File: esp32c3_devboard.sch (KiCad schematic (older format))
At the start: 0 parts

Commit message: Update schematic with ESP32 module, power supply and USB to serial
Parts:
- added C? (x5): 0.1uF, symbol Device:C_Small
- added C? (x2): 1uF, symbol Device:C_Small
- added C? (x3): 10uF, symbol Device:C_Small
- added D? (x2): D_Schottky, symbol Device:D_Schottky_Small
- added D?: YELLOW_LED, symbol Device:LED_Small
- added D?: RED_LED, symbol Device:LED_Small
- added J?: UART USB, symbol Connector:USB_B_Micro
- added J?: JTAG USB, symbol Connector:USB_B_Micro
- added J? (x2): Conn_01x15_Male, symbol Connector_Generic:Conn_01x15
- added R?: 10K, symbol Device:R_Small
- added R?: 800R, symbol Device:R_Small
- added R?: 1.7K, symbol Device:R_Small
- added SW? (x2): RSTn, symbol Switch:SW_Push
- added TP? (x12): TestPoint, symbol Connector:TestPoint
- added U?: ESP32-C3-MINI-1, Espressif:ESP32-C3-MINI-1, symbol Espressif:ESP32-C3-MINI-1
- added U?: AMS1117, Package_TO_SOT_SMD:SOT-223-3_TabPin2, symbol Regulator_Linear:AMS1117-3.3
- added U?: CH340E, Package_SO:MSOP-10_3x3mm_P0.5mm, symbol Interface_USB:CH340E
- added U?: SRV05-4, Package_TO_SOT_SMD:SOT-23-6, symbol Power_Protection:SRV05-4
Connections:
- new net: C?.1, U?.10 (V3)
- new net: D?.2 (A), R?.2 (x2)
- new net +3V3: C?.1, C?.1, C?.1, C?.1, J?.2 (Pin_2), J?.3 (Pin_3), R?.1, R?.1, TP?.1, U?.2 (VO), U?.3 (3V3)
- new net +5VL: D?.2 (A), J?.1 (VBUS), TP?.1
- new net +5VP: D?.2 (A), J?.1 (VBUS), TP?.1
- new net CHIP_PU: C?.1, J?.7 (Pin_7), R?.2, SW?.2, TP?.1, U?.8 (EN/CHIP_PU)
- new net GND: C?.2, C?.2, C?.2, C?.2, C?.2, C?.2, C?.2, C?.2, C?.2, C?.2, D?.1 (K), D?.1 (K), J?.1 (Pin_1), J?.1 (Pin_1), J?.12 (Pin_12), J?.12 (Pin_12), J?.15 (Pin_15), J?.15 (Pin_15), J?.4 (Pin_4), J?.5 (GND), J?.5 (GND), J?.6 (Pin_6), J?.7 (Pin_7), J?.8 (Pin_8), SW?.1, SW?.1, U?.1 (GND), U?.1 (GND), U?.11 (GND), U?.14 (GND), U?.2 (GND), U?.2 (VN), U?.3 (GND), U?.36 (GND)
- new net GPIO0: J?.9 (Pin_9), U?.12 (GPIO0/ADC1_CH0/XTAL_32K_P)
- new net GPIO1: J?.10 (Pin_10), U?.13 (GPIO1/ADC1_CH1/XTAL_32K_N)
- new net GPIO10: J?.11 (Pin_11), U?.16 (GPIO10)
- new net GPIO18: J?.13 (Pin_13), J?.2 (D-), U?.26 (GPIO18/USB_D-), U?.6 (IO4)
- new net GPIO19: J?.14 (Pin_14), J?.3 (D+), U?.27 (GPIO19/USB_D+), U?.4 (IO3)
- new net GPIO2: J?.4 (Pin_4), TP?.1, U?.5 (GPIO2/ADC1_CH2)
- new net GPIO3: J?.5 (Pin_5), U?.6 (GPIO3/ADC1_CH3)
- new net GPIO4: J?.11 (Pin_11), U?.18 (GPIO4/ADC1_CH4)
- new net GPIO5: J?.10 (Pin_10), U?.19 (GPIO5/ADC2_CH0)
- new net GPIO6: J?.9 (Pin_9), U?.20 (GPIO6)
- new net GPIO7: J?.8 (Pin_8), U?.21 (GPIO7)
- new net GPIO8: J?.6 (Pin_6), R?.1, TP?.1, U?.22 (GPIO8)
- new net GPIO9: J?.5 (Pin_5), SW?.2, TP?.1, U?.23 (GPIO9)
- new net RXD_3V3: J?.3 (Pin_3), TP?.1, U?.30 (GPIO20/U0RXD)
- new net RXD_5V: TP?.1, U?.9 (RXD)
- new net TXD_3V3: J?.2 (Pin_2), TP?.1, U?.31 (GPIO21/U0TXD)
- new net TXD_5V: TP?.1, U?.8 (TXD)
- new net UART_USB_D+: J?.3 (D+), U?.1 (IO1), U?.1 (UD+)
- new net UART_USB_D-: J?.2 (D-), U?.2 (UD-), U?.3 (IO2)
- new net VCC: C?.1, C?.1, C?.1, C?.1, D?.1 (K), D?.1 (K), J?.13 (Pin_13), J?.14 (Pin_14), TP?.1, U?.3 (VI), U?.5 (VP), U?.7 (VCC)
- no-connect marks 0 -> 21
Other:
- note added: "2 mA LED current"
- note added: "5V to 3.3V LDO"
- note added: "ESP32-C3-MINI-1 module"
- note added: "Input power supply selection"
- note added: "JTAG USB connector"
- note added: "Pin headers"
- note added: "Power indicator LED"
- note added: "Power supply test points:"
- note added: "Reset button"
- note added: "Strapping pins"
- note added: "Strapping pins test points:"
- note added: "Test points"
- note added: "UART 5V to 3.3V level shifter"
- note added: "UART USB connector"
- note added: "UART test points:"
- note added: "USB ESD protection"
- note added: "USB to UART"
- note added: "User LED and button"

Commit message: Place components on PCB
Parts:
- removed C? (x2): 0.1uF, symbol Device:C_Small
- removed C?: 1uF, symbol Device:C_Small
- removed TP? (x2): TestPoint, symbol Connector:TestPoint
- removed U?: CH340E, Package_SO:MSOP-10_3x3mm_P0.5mm, symbol Interface_USB:CH340E
- added C10: 10uF, Capacitor_SMD:C_0805_2012Metric, symbol Device:C_Small
- added C8: 1uF, Capacitor_SMD:C_0402_1005Metric, symbol Device:C_Small
- added C9: 0.1uF, Capacitor_SMD:C_0402_1005Metric, symbol Device:C_Small
- added NT1: Net-Tie_3, NetTie:NetTie-3_SMD_Pad2.0mm, symbol Device:Net-Tie_3
- added R3: 10K, Resistor_SMD:R_0603_1608Metric, symbol Device:R_Small
- added R5: 24K, Resistor_SMD:R_0603_1608Metric, symbol Device:R_Small
- added R6: 47K, Resistor_SMD:R_0603_1608Metric, symbol Device:R_Small
- added R7: 4K7, Resistor_SMD:R_0603_1608Metric, symbol Device:R_Small
- added U4: CP2102N-A01-GQFN28, Package_DFN_QFN:QFN-28-1EP_5x5mm_P0.5mm_EP3.35x3.35mm, symbol Interface_USB:CP2102N-A01-GQFN28
- C1, C4, C7: renamed from C?; footprint (none) -> Capacitor_SMD:C_0805_2012Metric
- C2, C3: renamed from C?; footprint (none) -> Capacitor_SMD:C_0402_1005Metric
- C5, C6: renamed from C?; footprint (none) -> Capacitor_SMD:C_0603_1608Metric
- D1, D2: renamed from D?; footprint (none) -> Diode_SMD:D_SOD-323
- D3, D4: renamed from D?; footprint (none) -> LED_SMD:LED_0805_2012Metric
- J1, J2: renamed from J?; footprint (none) -> Connector_USB:USB_Micro-B_Molex-105017-0001
- J3, J4: renamed from J?; footprint (none) -> Connector_PinHeader_2.54mm:PinHeader_1x15_P2.54mm_Vertical
- R1: renamed from R?; footprint (none) -> Resistor_SMD:R_0603_1608Metric
- R2: renamed from R?; value 800R -> 1K; footprint (none) -> Resistor_SMD:R_0603_1608Metric
- R4: renamed from R?; value 1.7K -> 1.1K; footprint (none) -> Resistor_SMD:R_0603_1608Metric
- SW1: renamed from SW?; value RSTn -> SW_RSTN; footprint (none) -> Button_Switch_SMD:SW_Push_1P1T_NO_6x6mm_H9.5mm
- SW2: renamed from SW?; value RSTn -> SW_USR; footprint (none) -> Button_Switch_SMD:SW_Push_1P1T_NO_6x6mm_H9.5mm
- TP1: renamed from TP?; value TestPoint -> TP_5V_UART_USB; footprint (none) -> TestPoint:TestPoint_Pad_D1.0mm
- TP10: renamed from TP?; value TestPoint -> TP_BOOT_GPIO9; footprint (none) -> TestPoint:TestPoint_Pad_D1.0mm
- TP2: renamed from TP?; value TestPoint -> TP_5V_JTAG_USB; footprint (none) -> TestPoint:TestPoint_Pad_D1.0mm
- TP3: renamed from TP?; value TestPoint -> TP_5V; footprint (none) -> TestPoint:TestPoint_Pad_D1.0mm
- TP4: renamed from TP?; value TestPoint -> TP_3V3; footprint (none) -> TestPoint:TestPoint_Pad_D1.0mm
- TP5: renamed from TP?; value TestPoint -> TP_UART_TXD; footprint (none) -> TestPoint:TestPoint_Pad_D1.0mm
- TP6: renamed from TP?; value TestPoint -> TP_UART_RXD; footprint (none) -> TestPoint:TestPoint_Pad_D1.0mm
- TP7: renamed from TP?; value TestPoint -> TP_CHIP_PU; footprint (none) -> TestPoint:TestPoint_Pad_D1.0mm
- TP8: renamed from TP?; value TestPoint -> TP_BOOT_GPIO2; footprint (none) -> TestPoint:TestPoint_Pad_D1.0mm
- TP9: renamed from TP?; value TestPoint -> TP_BOOT_GPIO8; footprint (none) -> TestPoint:TestPoint_Pad_D1.0mm
- gave numbers to parts that had none: 3
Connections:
- net RXD_5V is gone; now on net RXD: TP6.1
- net TXD_5V is gone; now on net TXD: TP5.1
- net +3V3: now also C10.1, C9.1, R3.1, R7.1, U4.6 (VDD), U4.7 (REGIN)
- net +5VP: now also R5.1
- net CHIP_PU: now also U4.24 (~RTS)
- net GND: now also C10.2, C8.2, C9.2, NT1.2, R6.2, U4.29 (GND), U4.3 (GND); no longer J1.5 (GND), J2.5 (GND)
- net GPIO8: now also R3.2
- net UART_USB_D+: now also U2.6 (IO4), U4.4 (D+); no longer U2.1 (IO1)
- net UART_USB_D-: now also U2.4 (IO3), U4.5 (D-); no longer U2.3 (IO2)
- net YELLOW_LED_PU: now reaches D4.2 (A), R4.2
- net RED_LED_PU: now reaches D3.2 (A), R2.2
- net GPIO18 renamed JTAG_USB_D-
- net JTAG_USB_D-: now also U2.1 (IO1); no longer U2.6 (IO4)
- net GPIO19 renamed JTAG_USB_D+
- net JTAG_USB_D+: now also U2.3 (IO2); no longer U2.4 (IO3)
- net GPIO9 renamed DTR
- net DTR: now also U4.28 (~DTR)
- net RXD_3V3 renamed RXD
- net RXD: now also U4.26 (TXD)
- net TXD_3V3 renamed TXD
- net TXD: now also U4.25 (RXD)
- net VCC renamed +5V
- new net GND1: J1.5 (GND), NT1.3
- new net GND2: J2.5 (GND), NT1.1
- new net RSTb: R7.2, U4.9 (~RSTb)
- new net VBUS: C8.1, R5.2, R6.1, U4.8 (VBUS)
- no-connect marks 21 -> 34
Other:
- note added: "GPIO8 needs to be pulled up\nin order to enter bootloader"
- note added: "Power indication LED"
- note added: "RTS should be connected to CHIP_PU\n\nDTR should be connected to GPIO9"
- note added: "TXD and RXD crossover intentional"
- note added: "UART_USB and JTAG_USB grounds are tied"
- note added: "Voltage divider needed for limiting VBUS\nvoltage when 3V3 is not connected\n\nCapacitor is here to delay rising of VBUS\nvoltage until LDO enables the 3V3 output"
- note removed: "Power indicator LED"
- note removed: "UART 5V to 3.3V level shifter"
- moved on the sheet: C3, C4, C5, C6, C7, D1, D2, D3, D4, J1, J3, J4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

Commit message: Add pullup on GPIO2 strapping pin
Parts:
- added R8: 10K, Resistor_SMD:R_0603_1608Metric, symbol Device:R_Small
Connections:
- net +3V3: now also R8.1
- net GPIO2: now also R8.2
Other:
- note added: "GPIO2 should be pulled up\n\nRTS should be connected to CHIP_PU\n\nDTR should be connected to GPIO9"
- note removed: "RTS should be connected to CHIP_PU\n\nDTR should be connected to GPIO9"
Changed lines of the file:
@@
 Text GLabel 2550 7050 0    35   Input ~ 0
 DTR
-Text Notes 2250 6450 0    31   ~ 0
-RTS should be connected to CHIP_PU\n\nDTR should be connected to GPIO9
 Text Notes 9950 4100 0    31   ~ 0
 TXD and RXD crossover intentional
@@
 Text Label 5900 7050 0    35   ~ 0
 YELLOW_LED_PU
+$Comp
+L Device:R_Small R8
+U 1 1 6332661E
+P 3200 6550
+F 0 "R8" H 3250 6650 35  0000 L CNN
+F 1 "10K" H 3250 6500 35  0000 L CNN
+F 2 "Resistor_SMD:R_0603_1608Metric" H 3200 6550 50  0001 C CNN
+F 3 "~" H 3200 6550 50  0001 C CNN
+	1    3200 6550
+	1    0    0    -1
+$EndComp
+$Comp
+L power:+3.3V #PWR06
+U 1 1 63326CD9
+P 3200 6400
+F 0 "#PWR06" H 3200 6250 50  0001 C CNN
+F 1 "+3.3V" H 3200 6550 35  0000 C CNN
+F 2 "" H 3200 6400 50  0001 C CNN
+F 3 "" H 3200 6400 50  0001 C CNN
+	1    3200 6400
+	1    0    0    -1
+$EndComp
+Text Notes 2100 6550 0    31   ~ 0
+GPIO2 should be pulled up\n\nRTS should be connected to CHIP_PU\n\nDTR should be connected to GPIO9
+Wire Wire Line
+	3200 6650 3400 6650
+Wire Wire Line
+	3200 6400 3200 6450
 $EndSCHEMATC

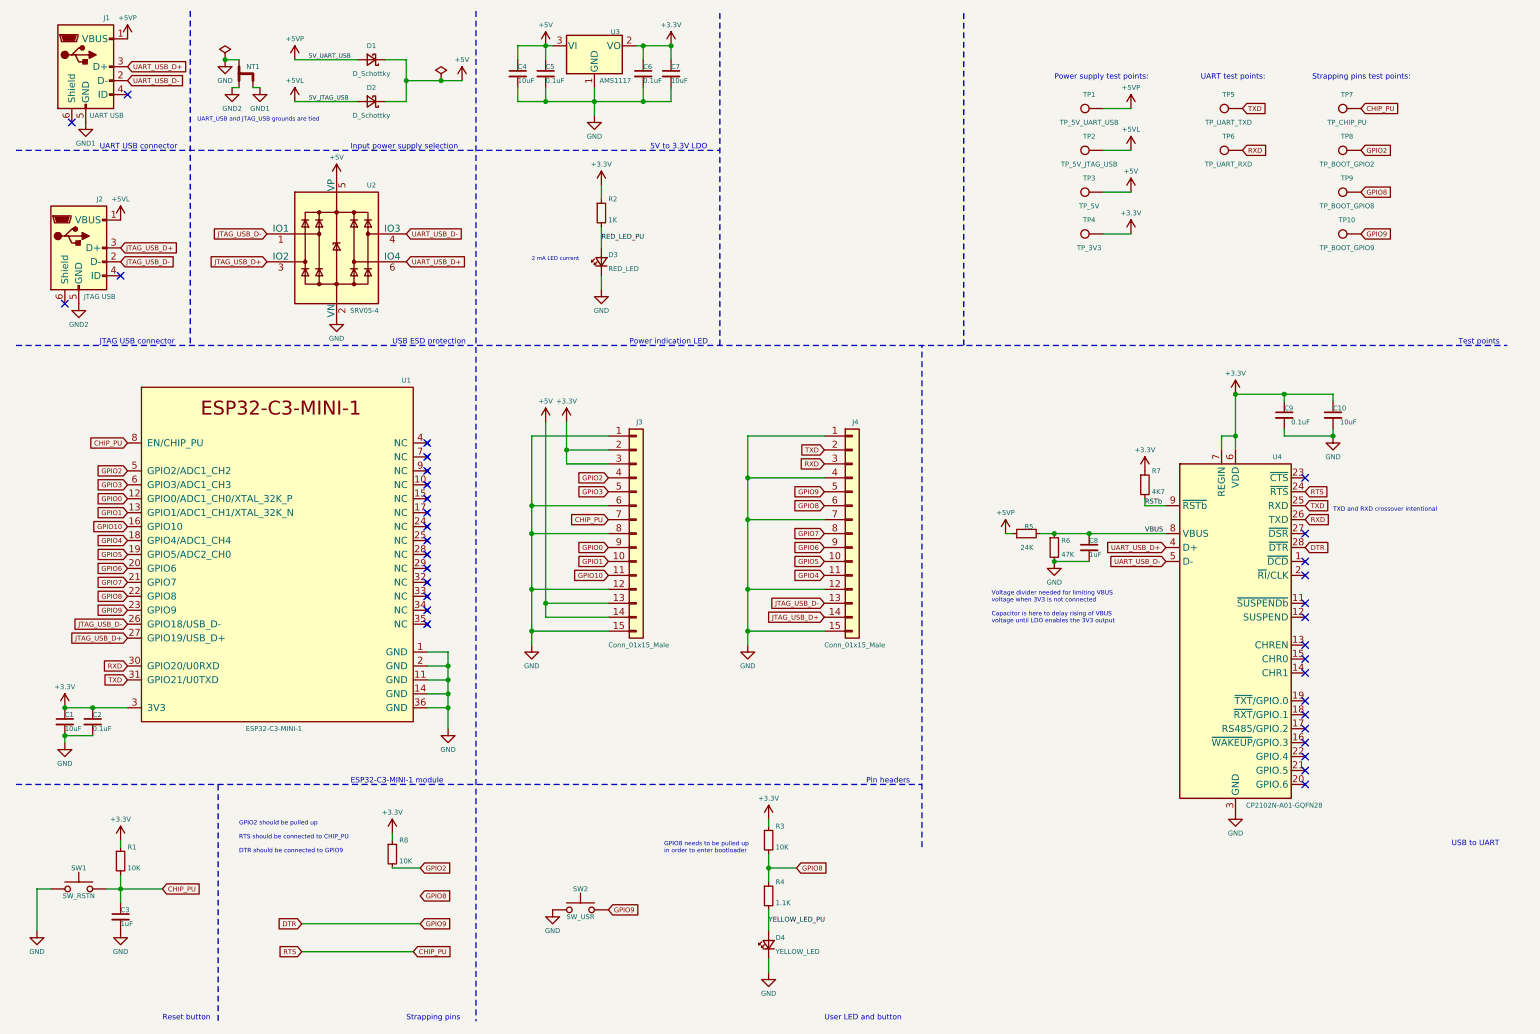
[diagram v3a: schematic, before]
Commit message: Add micro USB step files
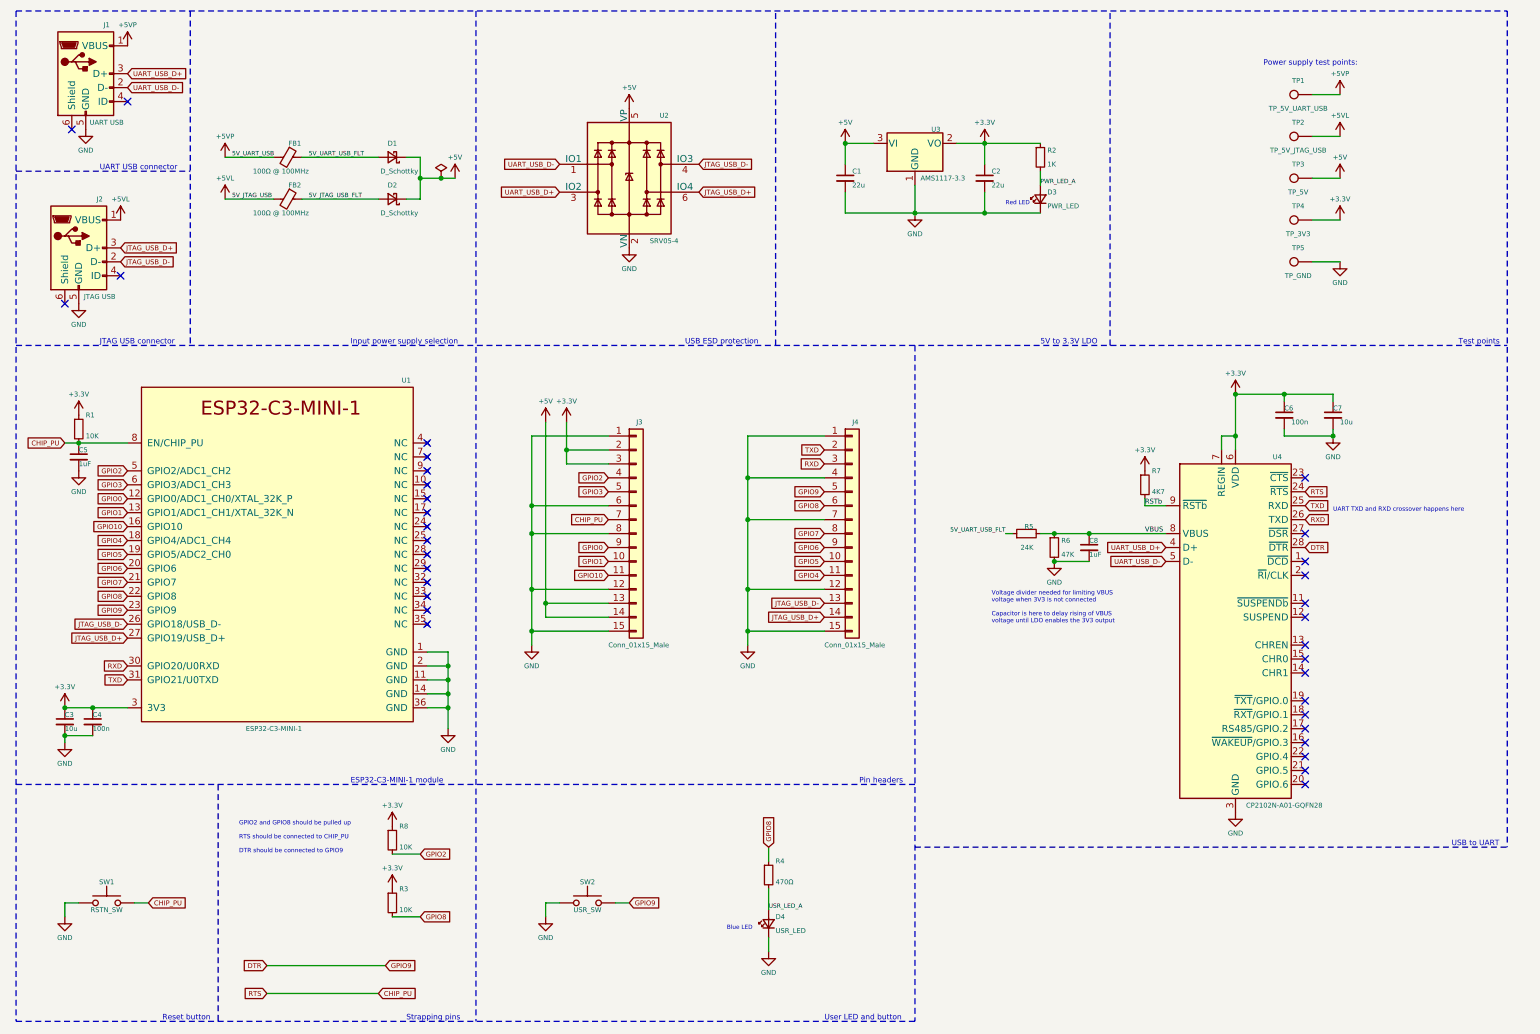
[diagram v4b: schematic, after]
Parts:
- removed C5, C6: 0.1uF, Capacitor_SMD:C_0603_1608Metric, symbol Device:C_Small
- removed NT1: Net-Tie_3, NetTie:NetTie-3_SMD_Pad2.0mm, symbol Device:Net-Tie_3
- removed TP10: TP_BOOT_GPIO9, TestPoint:TestPoint_Pad_D1.0mm, symbol Connector:TestPoint
- removed TP6: TP_UART_RXD, TestPoint:TestPoint_Pad_D1.0mm, symbol Connector:TestPoint
- removed TP7: TP_CHIP_PU, TestPoint:TestPoint_Pad_D1.0mm, symbol Connector:TestPoint
- removed TP8: TP_BOOT_GPIO2, TestPoint:TestPoint_Pad_D1.0mm, symbol Connector:TestPoint
- removed TP9: TP_BOOT_GPIO8, TestPoint:TestPoint_Pad_D1.0mm, symbol Connector:TestPoint
- added FB1, FB2: 100Ω @ 100MHz, Inductor_SMD:L_0805_2012Metric, symbol Device:Ferrite_Bead_Small
- C1: renamed from C4; value 10uF -> 22u; footprint Capacitor_SMD:C_0805_2012Metric -> Capacitor_SMD:C_1206_3216Metric; LCSC (none) -> C12891
- C2: renamed from C7; value 10uF -> 22u; footprint Capacitor_SMD:C_0805_2012Metric -> Capacitor_SMD:C_1206_3216Metric; LCSC (none) -> C12891
- C3: renamed from C1; value 10uF -> 10u; LCSC (none) -> C440198
- C4: renamed from C2; value 0.1uF -> 100n; LCSC (none) -> C307331
- C5: renamed from C3; LCSC (none) -> C52923
- C6: renamed from C9; value 0.1uF -> 100n; LCSC (none) -> C307331
- C7: renamed from C10; value 10uF -> 10u; LCSC (none) -> C440198
- C8: LCSC (none) -> C52923
- D1, D2: LCSC (none) -> C191023
- D3: value RED_LED -> PWR_LED; footprint LED_SMD:LED_0805_2012Metric -> LED_SMD:LED_0603_1608Metric; LCSC (none) -> C2286
- D4: value YELLOW_LED -> USR_LED; footprint LED_SMD:LED_0805_2012Metric -> LED_SMD:LED_0603_1608Metric; LCSC (none) -> C72041
- J1, J2: footprint Connector_USB:USB_Micro-B_Molex-105017-0001 -> Connector_USB:USB_Micro-B_Wuerth_629105150521; LCSC (none) -> C2926996
- R1, R3, R8: footprint Resistor_SMD:R_0603_1608Metric -> Resistor_SMD:R_0402_1005Metric; LCSC (none) -> C25744
- R2: LCSC (none) -> C21190
- R4: value 1.1K -> 470Ω; LCSC (none) -> C23179
- R5: footprint Resistor_SMD:R_0603_1608Metric -> Resistor_SMD:R_0402_1005Metric; LCSC (none) -> C25769
- R6: footprint Resistor_SMD:R_0603_1608Metric -> Resistor_SMD:R_0402_1005Metric; LCSC (none) -> C25792
- R7: footprint Resistor_SMD:R_0603_1608Metric -> Resistor_SMD:R_0402_1005Metric; LCSC (none) -> C25900
- SW1: value SW_RSTN -> RSTN_SW; footprint Button_Switch_SMD:SW_Push_1P1T_NO_6x6mm_H9.5mm -> Button_Switch_SMD:SW_SPST_TL3342; LCSC (none) -> C318884
- SW2: value SW_USR -> USR_SW; footprint Button_Switch_SMD:SW_Push_1P1T_NO_6x6mm_H9.5mm -> Button_Switch_SMD:SW_SPST_TL3342; LCSC (none) -> C318884
- TP5: value TP_UART_TXD -> TP_GND
- U1: LCSC (none) -> C2838502
- U2: LCSC (none) -> C85364
- U3: value AMS1117 -> AMS1117-3.3; LCSC (none) -> C6186
- U4: LCSC (none) -> C6568
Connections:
- net GND1 is gone; now on net GND: J1.5 (GND)
- net GND2 is gone; now on net GND: J2.5 (GND)
- net +5VL: now also FB2.2; no longer D2.2 (A)
- net +5VP: now also FB1.2; no longer D1.2 (A), R5.1
- net GND: now also TP5.1
- net JTAG_USB_D+: now also U2.6 (IO4); no longer U2.3 (IO2)
- net JTAG_USB_D-: now also U2.4 (IO3); no longer U2.1 (IO1)
- net TXD: no longer TP5.1
- net UART_USB_D+: now also U2.3 (IO2); no longer U2.6 (IO4)
- net UART_USB_D-: now also U2.1 (IO1); no longer U2.4 (IO3)
- net RED_LED_PU renamed PWR_LED_A
- net YELLOW_LED_PU renamed USR_LED_A
- new net 5V_JTAG_USB_FLT: D2.2 (A), FB2.1
- new net 5V_UART_USB_FLT: D1.2 (A), FB1.1, R5.1
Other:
- note added: "Blue LED"
- note added: "GPIO2 and GPIO8 should be pulled up\n\nRTS should be connected to CHIP_PU\n\nDTR should be connected to GPIO9"
- note added: "Red LED"
- note added: "UART TXD and RXD crossover happens here"
- note removed: "2 mA LED current"
- note removed: "GPIO2 should be pulled up\n\nRTS should be connected to CHIP_PU\n\nDTR should be connected to GPIO9"
- note removed: "GPIO8 needs to be pulled up\nin order to enter bootloader"
- note removed: "Power indication LED"
- note removed: "Strapping pins test points:"
- note removed: "TXD and RXD crossover intentional"
- note removed: "UART test points:"
- note removed: "UART_USB and JTAG_USB grounds are tied"
- moved on the sheet: C1, C2, C5, D1, D2, D3, D4, J1, R1, R2, R4, R8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

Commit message: Change button silkscreen labels to RST and BOOT
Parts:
- SW1: value RSTN_SW -> RST
- SW2: value USR_SW -> BOOT
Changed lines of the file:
@@
 P 1150 6900
 F 0 "SW1" H 1150 7050 35  0000 C CNN
-F 1 "RSTN_SW" H 1150 6850 35  0000 C CNN
+F 1 "RST" H 1150 6850 35  0000 C CNN
 F 2 "Button_Switch_SMD:SW_SPST_TL3342" H 1150 7100 50  0001 C CNN
 F 3 "https://datasheet.lcsc.com/lcsc/2002271431_XKB-Connectivity-TS-1187A-B-A-B_C318884.pdf" H 1150 7100 50  0001 C CNN
@@
 P 4600 6900
 F 0 "SW2" H 4600 7050 35  0000 C CNN
-F 1 "USR_SW" H 4600 6850 35  0000 C CNN
+F 1 "BOOT" H 4600 6850 35  0000 C CNN
 F 2 "Button_Switch_SMD:SW_SPST_TL3342" H 4600 7100 50  0001 C CNN
 F 3 "https://datasheet.lcsc.com/lcsc/2002271431_XKB-Connectivity-TS-1187A-B-A-B_C318884.pdf" H 4600 7100 50  0001 C CNN
